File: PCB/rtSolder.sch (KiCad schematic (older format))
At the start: 44 parts, among them J1 AudioJack3, J2 Conn_01x05, J3 Jack-DC, Q1 DMP4013LFG-7, SW1 Schurter_1301.9319, SW2 Schurter_1301.9319, U1 LMR14050SDDAR, U2 MIC5233-3.3YS, U3 PIC16F1788-xML, U4 OLED_128x32, U5 TLV333IDCKR

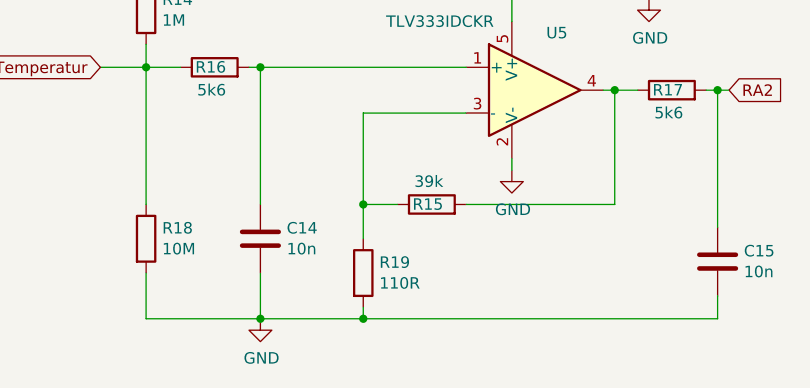
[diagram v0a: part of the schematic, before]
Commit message: adjust temp measurement
changed R19 to 150R
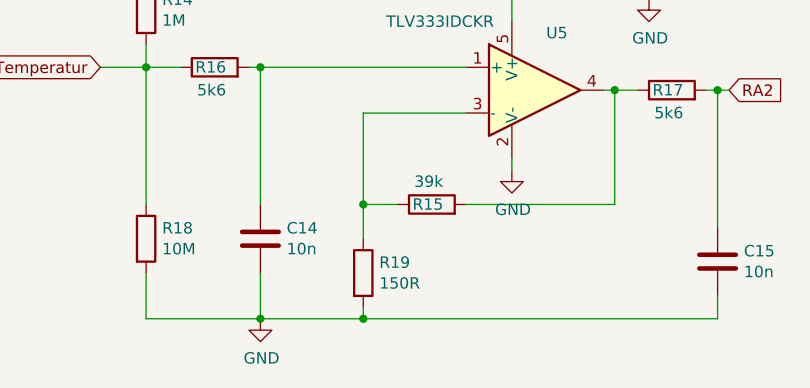
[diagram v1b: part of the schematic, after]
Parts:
- R19: value 110R -> 150R
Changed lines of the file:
@@
 P 2850 7200
 F 0 "R19" H 2920 7246 50  0000 L CNN
-F 1 "110R" H 2920 7155 50  0000 L CNN
+F 1 "150R" H 2920 7155 50  0000 L CNN
 F 2 "Resistor_SMD:R_0603_1608Metric" V 2780 7200 50  0001 C CNN
 F 3 "~" H 2850 7200 50  0001 C CNN
